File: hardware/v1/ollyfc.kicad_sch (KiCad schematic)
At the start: 64 parts, among them J1 Conn_01x06, J5 Conn_02x05_Odd_Even, Q2 MMBT3904, Q3 MMBT3904, SW2 SW_Push, SW4 MODE1, SW5 MODE1, U3 STM32F411RETx, U6 W25Q128JVS, Y1 X322516MLB4SI

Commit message: some hardware designs
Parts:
- removed TP1, TP10, TP11, TP12, TP13, TP14, TP15, TP16, TP17, TP18, TP19, TP2, TP20, TP21, TP22, TP3, TP4, TP5, TP6, TP7, TP8, TP9: TestPoint, TestPoint:TestPoint_THTPad_D1.0mm_Drill0.5mm, symbol Connector:TestPoint
- added J13: Conn_01x05, Connector_PinHeader_2.54mm:PinHeader_1x05_P2.54mm_Vertical, symbol Connector_Generic:Conn_01x05
- added R15: 5K1, Resistor_SMD:R_0402_1005Metric, symbol Device:R_Small
- added SW3: SW_Push, Button_Switch_THT:SW_PUSH_6mm, symbol Switch:SW_Push
- BT1: footprint LCSC:BAT-TH_MY-927-01 -> Battery:BatteryHolder_Keystone_3002_1x2032
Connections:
- net +3V3: now also SW3.2
- net ACCEL_INT1: now also U3.26 (PB0); no longer U3.57 (PB5)
- net CSB_ACCEL: now also U3.25 (PC5); no longer U3.17 (PA3)
- net GND: now also R15.1
- net GYRO_INT4: now also U3.24 (PC4); no longer U3.16 (PA2)
- net PWR_STATE: now also U3.21 (PA5), U3.8 (PC0); no longer U3.39 (PC8)
- net USART2_CTS: now reaches U3.14 (PA0)
- net USART2_CTS: now also J13.1 (Pin_1)
- net USART2_RTS: now reaches U3.15 (PA1)
- net USART2_RTS: now also J13.2 (Pin_2)
- net USART2_CK: now reaches U3.20 (PA4)
- net USART2_CK: now also J13.5 (Pin_5)
- net GNSS_TIMEP: now reaches U3.27 (PB1)
- net GNSS_INT: now reaches U3.28 (PB2)
- net MAG_DRDY: now reaches U3.36 (PB15)
- net GNSS_CS: now reaches U3.43 (PA10)
- net BOOT0: now reaches U3.60 (BOOT0)
- net BOOT0: now also R15.2, SW3.1
- net FG_ALERT: no longer names the net of U3.33 (PB12)
- net FG_QSTRT renamed MAG_CS
- new net MAG_INT: U3.39 (PC8)
- new net USART2_RX: J13.4 (Pin_4), U3.17 (PA3)
- new net USART2_TX: J13.3 (Pin_3), U3.16 (PA2)
- no-connect marks 20 -> 7

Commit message: Route another?
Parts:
- removed R17: 5K1, Resistor_SMD:R_0402_1005Metric, symbol Device:R_Small
- added H6: MountingHole, MountingHole:MountingHole_3.2mm_M3, symbol Mechanical:MountingHole
- added J12: Conn_01x04, Connector_PinHeader_2.54mm:PinHeader_1x05_P2.54mm_Vertical, symbol Connector_Generic:Conn_01x05
- added J14, J15: Conn_01x04, Connector_PinHeader_2.54mm:PinHeader_1x04_P2.54mm_Vertical, symbol Connector_Generic:Conn_01x04
- added R1: 5K1, Resistor_SMD:R_0402_1005Metric, symbol Device:R_Small
- J13: value Conn_01x05 -> Conn_01x04; footprint Connector_PinHeader_2.54mm:PinHeader_1x05_P2.54mm_Vertical -> Connector_PinHeader_2.54mm:PinHeader_1x04_P2.54mm_Vertical; symbol Connector_Generic:Conn_01x05 -> Connector_Generic:Conn_01x04
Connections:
- net MAG_CS is gone; now on net LED2: U3.35 (PB14)
- net +3V3: now also J14.2 (Pin_2), J15.2 (Pin_2), R1.1
- net ACCEL_INT1: now also U3.4 (PC15); no longer U3.26 (PB0)
- net ACCEL_INT2: now also U3.3 (PC14); no longer U3.61 (PB8)
- net CSB_ACCEL: no longer U3.25 (PC5)
- net CSB_GYRO: no longer U3.23 (PA7)
- net FMEM_CS: now also U3.20 (PA4), J12.1 (Pin_1); no longer U3.50 (PA15)
- net FMEM_HOLD: now also U3.26 (PB0), J12.4 (Pin_4); no longer U3.56 (PB4)
- net GND: now also J14.1 (Pin_1), J15.1 (Pin_1)
- net GNSS_CS: no longer U3.43 (PA10)
- net GNSS_INT: now also U3.52 (PC11); no longer U3.28 (PB2)
- net GNSS_TIMEP: now also U3.51 (PC10); no longer U3.27 (PB1)
- net GYRO_INT3: now also U3.57 (PB5); no longer U3.22 (PA6)
- net GYRO_INT4: now also U3.61 (PB8); no longer U3.24 (PC4)
- net I2C2_SCL: now also R9.2, J15.3 (Pin_3); no longer R8.2
- net I2C2_SDA: now also R8.2, J15.4 (Pin_4); no longer R9.2
- net I2C3_SCL: no longer R12.2, U3.41 (PA8)
- net I2C3_SDA: no longer U3.40 (PC9)
- net LED1: now also U3.38 (PC7); no longer U3.2 (PC13)
- net LED2: no longer U3.3 (PC14)
- net MAG_DRDY: now also U3.9 (PC1); no longer U3.36 (PB15)
- net MAG_INT: now also U3.2 (PC13); no longer U3.39 (PC8)
- net MODE1: now also U3.10 (PC2); no longer U3.58 (PB6)
- net MODE2: now also U3.39 (PC8); no longer U3.59 (PB7)
- net NRST: no longer J5.10 (Pin_10)
- net PRES_INT: now also U3.27 (PB1); no longer U3.9 (PC1)
- net PWR_STATE: now also U3.37 (PC6); no longer U3.21 (PA5), U3.8 (PC0)
- net SPI1_MISO: now also U3.22 (PA6), J12.2 (Pin_2); no longer U3.52 (PC11)
- net SPI1_MOSI: now also U3.23 (PA7), J12.5 (Pin_5); no longer U3.53 (PC12)
- net SPI1_SCK: now also U3.21 (PA5), J12.3 (Pin_3); no longer U3.51 (PC10)
- net SPI2_MISO: no longer U3.11 (PC3)
- net SPI2_MOSI: no longer U3.10 (PC2)
- net SPI2_SCK: no longer U3.34 (PB13)
- net SWDCLK: no longer J5.4 (Pin_4), U3.49 (PA14)
- net SWDIO: no longer J5.2 (Pin_2), U3.46 (PA13)
- net SWO: no longer J5.6 (Pin_6), U3.55 (PB3)
- net USART6_RX: no longer Q3.3 (C), R5.1, U3.38 (PC7)
- net USART6_TX: no longer R2.1, U3.37 (PC6)
- net JTDI: now reaches J5.8 (Pin_8)
- net JTDI: now also U3.50 (PA15)
- net BUZZER renamed USART1_TX
- net USART1_TX: now also R2.1
- removed net USART2_CK: J13.5 (Pin_5), U3.20 (PA4)
- new net GNSS_RESET: U3.53 (PC12)
- new net I2C1_SCL: J14.3 (Pin_3), R12.2, U3.58 (PB6)
- new net I2C1_SDA: J14.4 (Pin_4), R1.2, U3.59 (PB7)
- new net JTCK_SWCLK: J5.4 (Pin_4), U3.49 (PA14)
- new net JTDO_SWO: J5.6 (Pin_6), U3.55 (PB3)
- new net JTMS_SWDIO: J5.2 (Pin_2), U3.46 (PA13)
- new net JTRST: J5.10 (Pin_10), U3.56 (PB4)
- new net USART1_RX: Q3.3 (C), R5.1, U3.43 (PA10)
- no-connect marks 7 -> 14
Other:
- moved on the sheet: R12, R7

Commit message: v2 PCB design
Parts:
- removed BT1: Battery_Cell, Battery:BatteryHolder_Keystone_3002_1x2032, symbol Device:Battery_Cell
- removed H6: MountingHole, MountingHole:MountingHole_3.2mm_M3, symbol Mechanical:MountingHole
- removed J15: Conn_01x04, Connector_PinHeader_2.54mm:PinHeader_1x04_P2.54mm_Vertical, symbol Connector_Generic:Conn_01x04
- J13: footprint Connector_PinHeader_2.54mm:PinHeader_1x04_P2.54mm_Vertical -> Connector_PinHeader_2.54mm:PinHeader_1x08_P2.54mm_Vertical; symbol Connector_Generic:Conn_01x04 -> Connector_Generic:Conn_01x08
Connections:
- net +3V3: now also J13.2 (Pin_2)
- net ACCEL_INT1: now also U3.3 (PC14); no longer U3.4 (PC15)
- net ACCEL_INT2: now also U3.4 (PC15); no longer U3.3 (PC14)
- net GND: now also J13.1 (Pin_1)
- net GNSS_RESET: now also U3.51 (PC10); no longer U3.53 (PC12)
- net GNSS_SAFEBOOT: now also U3.41 (PA8)
- net GNSS_TIMEP: now also U3.53 (PC12); no longer U3.51 (PC10)
- net I2C2_SCL: now also J13.3 (Pin_3)
- net I2C2_SDA: now also J13.4 (Pin_4)
- net MAG_DRDY: now also U3.8 (PC0); no longer U3.9 (PC1)
- net MAG_INT: now also U3.24 (PC4); no longer U3.2 (PC13)
- net MODE1: now also U3.27 (PB1); no longer U3.10 (PC2)
- net MODE2: now also U3.28 (PB2); no longer U3.39 (PC8)
- net PRES_INT: now also U3.9 (PC1); no longer U3.27 (PB1)
- net USART2_CTS: now also J13.5 (Pin_5); no longer J13.1 (Pin_1)
- net USART2_RTS: now also J13.6 (Pin_6); no longer J13.2 (Pin_2)
- net USART2_RX: now also J13.8 (Pin_8); no longer J13.4 (Pin_4)
- net USART2_TX: now also J13.7 (Pin_7); no longer J13.3 (Pin_3)
- net BUZZER: now reaches U3.36 (PB15)
- no-connect marks 14 -> 12
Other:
- note removed: "Test Points"
- moved on the sheet: R7

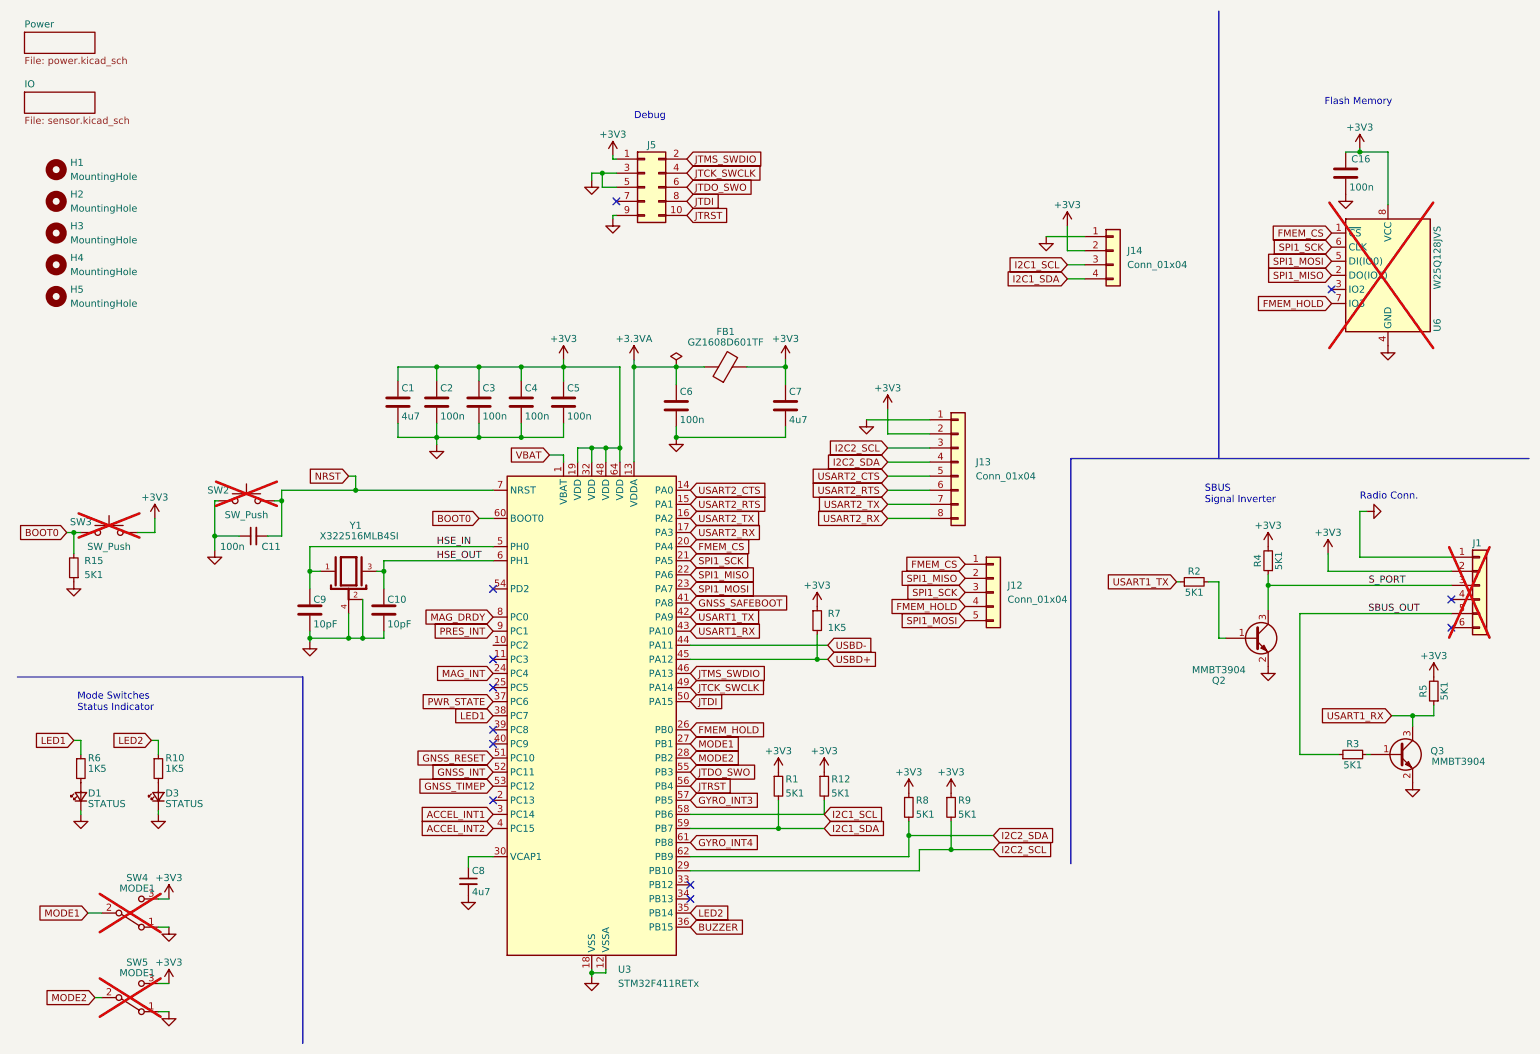
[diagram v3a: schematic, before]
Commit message: JLC part footprints
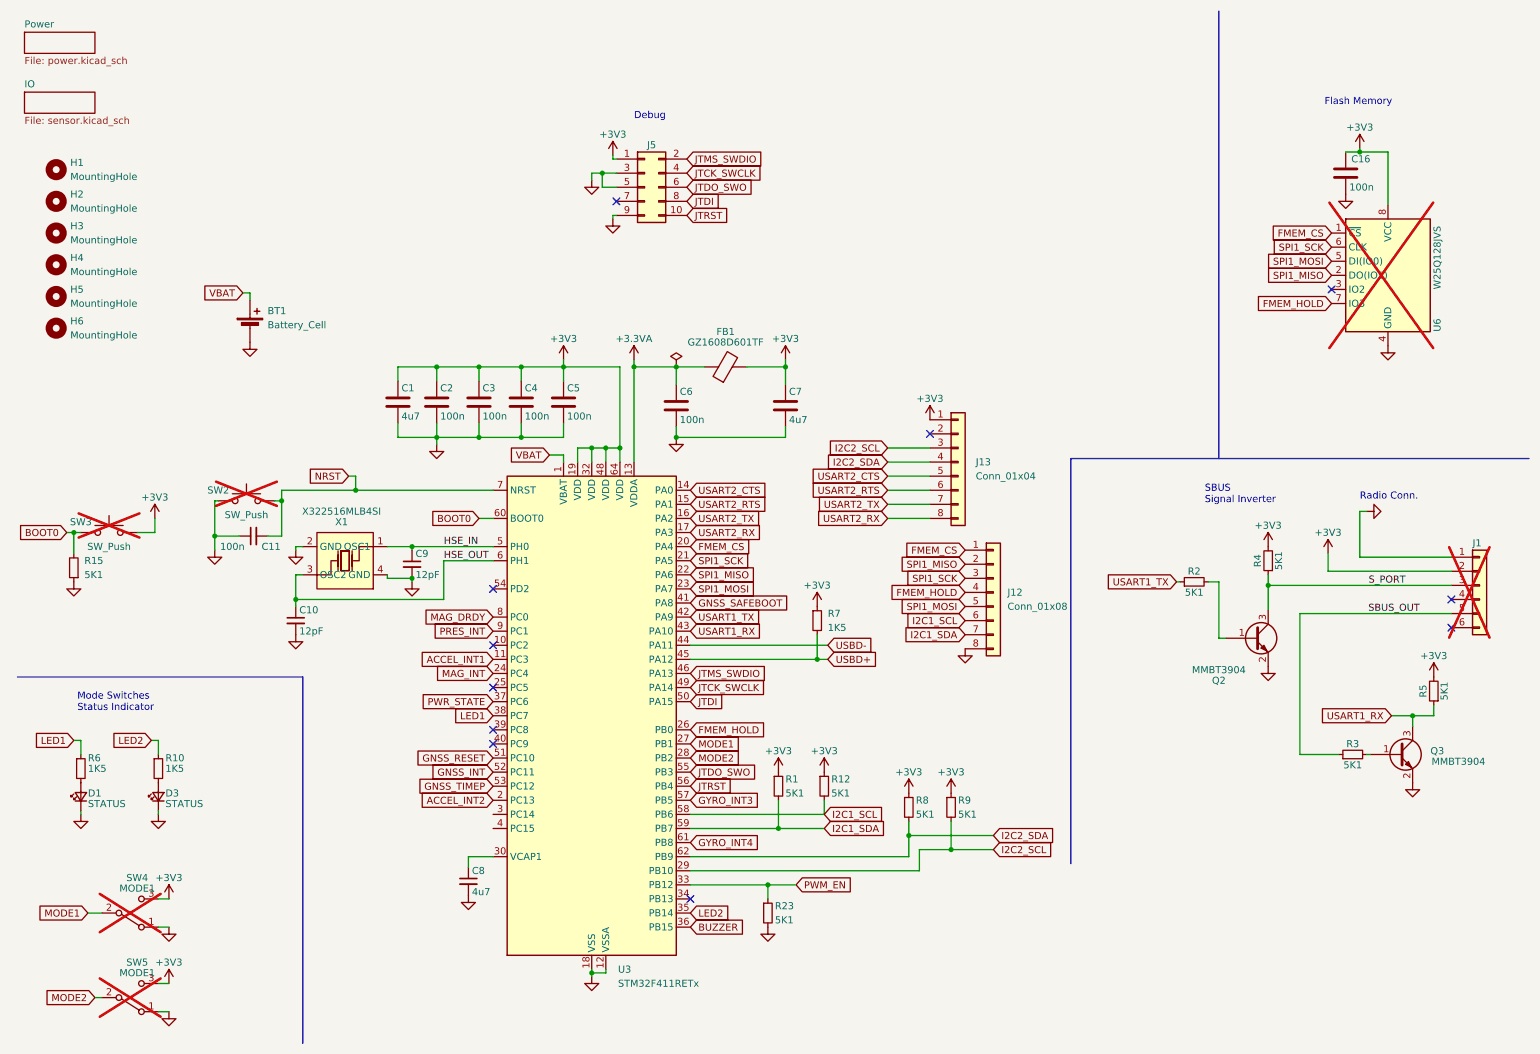
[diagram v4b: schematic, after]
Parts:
- removed C10, C9: 10pF, Capacitor_SMD:C_0402_1005Metric, symbol Device:C
- removed J14: Conn_01x04, Connector_PinHeader_2.54mm:PinHeader_1x04_P2.54mm_Vertical, symbol Connector_Generic:Conn_01x04
- removed Y1: X322516MLB4SI, Crystal:Crystal_SMD_SeikoEpson_TSX3225-4Pin_3.2x2.5mm, symbol Oscillator:X322516MLB4SI
- added BT1: Battery_Cell, Battery:BatteryHolder_LINX_BAT-HLD-012-SMT, symbol Device:Battery_Cell
- added C10, C9: 12pF, ofc_sym:C0402, symbol Device:C_Small
- added H6: MountingHole, MountingHole:MountingHole_3.2mm_M3, symbol Mechanical:MountingHole
- added R23: 5K1, Resistor_SMD:R_0402_1005Metric, symbol Device:R_Small
- added X1: X322516MLB4SI, ofc_sym:OSC-SMD_4P-L3.2-W2.5-BL, symbol ofc_sym:X322516MLB4SI
- J12: value Conn_01x04 -> Conn_01x08; footprint Connector_PinHeader_2.54mm:PinHeader_1x05_P2.54mm_Vertical -> Connector_PinHeader_2.54mm:PinHeader_1x08_P2.54mm_Vertical; symbol Connector_Generic:Conn_01x05 -> Connector_Generic:Conn_01x08
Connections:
- net +3V3: now also J13.1 (Pin_1); no longer J13.2 (Pin_2)
- net ACCEL_INT1: now also U3.11 (PC3); no longer U3.3 (PC14)
- net ACCEL_INT2: now also U3.2 (PC13); no longer U3.4 (PC15)
- net GND: now also J12.8 (Pin_8), BT1.2 (-), C10.2, C9.2, R23.2, X1.2 (GND), X1.4 (GND); no longer J13.1 (Pin_1)
- net HSE_IN: now also C9.1, X1.1 (OSC1)
- net HSE_OUT: now also C10.1, X1.3 (OSC2)
- net I2C1_SCL: now also J12.6 (Pin_6)
- net I2C1_SDA: now also J12.7 (Pin_7)
- net VBAT: now also BT1.1 (+)
- net PWM_EN: now reaches U3.33 (PB12)
- net PWM_EN: now also R23.1
- no-connect marks 12 -> 11
